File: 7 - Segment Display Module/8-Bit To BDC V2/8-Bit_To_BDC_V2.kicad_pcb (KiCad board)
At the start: 2 copper layers, 93 x 83 mm, 42 parts, among them J1 Conn_01x08_Pin, J2 Conn_01x02_Pin, U1 AT28C64B-15PU, U2 AT28C64B-15PU, U3 4056, U4 4056, U5 4056

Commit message: PCB Layout modification
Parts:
- removed R30: 330, Resistor_SMD:R_0805_2012Metric_Pad1.20x1.40mm_HandSolder
- added D10: US1M, Diode_SMD:D_SOD-323_HandSoldering, F.Cu at (82.4, 60.3)
- added D11: US1M, Diode_SMD:D_SOD-323_HandSoldering, F.Cu at (86.4, 60.3)
- added D4: US1M, Diode_SMD:D_SOD-323_HandSoldering, F.Cu at (58.4, 60.3)
- added D5: US1M, Diode_SMD:D_SOD-323_HandSoldering, F.Cu at (62.4, 60.3)
- added D6: US1M, Diode_SMD:D_SOD-323_HandSoldering, F.Cu at (66.4, 60.3)
- added D7: US1M, Diode_SMD:D_SOD-323_HandSoldering, F.Cu at (70.4, 60.3)
- added D8: US1M, Diode_SMD:D_SOD-323_HandSoldering, F.Cu at (74.4, 60.3)
- added D9: US1M, Diode_SMD:D_SOD-323_HandSoldering, F.Cu at (78.4, 60.3)
- added R22: 330, Resistor_SMD:R_0805_2012Metric_Pad1.20x1.40mm_HandSolder, F.Cu at (111.5, 52.0)
- moved J2 93.4 mm to (50.5, 31.7)
- moved R29 74.1 mm to (121.0, 30.1), turned to 180 degrees
- moved J1 72.2 mm to (50.0, 53.5)
- moved R28 67.3 mm to (121.0, 34.1), turned to 180 degrees
- moved R1 65.3 mm to (58.3, 64.1), turned to 90 degrees
- moved R9 64.7 mm to (70.0, 30.2)
- moved R10 63.7 mm to (70.0, 34.2)
- moved R11 62.8 mm to (70.0, 38.2)
- moved R2 62.4 mm to (62.3, 64.1), turned to 90 degrees
- moved R12 61.9 mm to (70.0, 42.2)
- moved R13 60.9 mm to (70.0, 46.2)
- moved R27 60.5 mm to (121.0, 38.1), turned to 180 degrees
- moved R14 60.0 mm to (70.0, 50.2)
- moved R3 59.6 mm to (66.3, 64.1), turned to 90 degrees
- moved R15 59.1 mm to (70.0, 54.2)
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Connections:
- J1 pad 1: 1 -> Net-(D4-A)
- J1 pad 2: 2 -> Net-(D5-A)
- J1 pad 3: 3 -> Net-(D6-A)
- J1 pad 4: 4 -> Net-(D7-A)
- J1 pad 5: 5 -> Net-(D8-A)
- J1 pad 6: 6 -> Net-(D9-A)
- J1 pad 7: 7 -> Net-(D10-A)
- J1 pad 8: 8 -> Net-(D11-A)
- R11 pad 1: Net-(U3-a) -> Net-(U3-c)
- R11 pad 2: H-A -> H-C
- R23 pad 1: Net-(U4-g) -> Net-(U5-a)
- R23 pad 2: T-G -> O-A
- R24 pad 1: Net-(U5-a) -> Net-(U5-b)
- R24 pad 2: O-A -> O-B
- R25 pad 1: Net-(U5-b) -> Net-(U5-c)
- R25 pad 2: O-B -> O-C
- R26 pad 1: Net-(U5-c) -> Net-(U5-d)
- R26 pad 2: O-C -> O-D
- R27 pad 1: Net-(U5-d) -> Net-(U5-e)
- R27 pad 2: O-D -> O-E
- R28 pad 1: Net-(U5-e) -> Net-(U5-f)
- R28 pad 2: O-E -> O-F
- R29 pad 1: Net-(U5-f) -> Net-(U5-g)
- R29 pad 2: O-F -> O-G
- R9 pad 1: Net-(U3-c) -> Net-(U3-a)
- R9 pad 2: H-C -> H-A
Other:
- board size 93 x 83 mm -> 99 x 67 mm

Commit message: Small changes
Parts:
- added REF**: MountingHole_2.7mm_M2.5_DIN965, MountingHole:MountingHole_2.7mm_M2.5_DIN965, F.Cu at (133.5, 71.0)
- added REF**: MountingHole_2.7mm_M2.5_DIN965, MountingHole:MountingHole_2.7mm_M2.5_DIN965, F.Cu at (134.0, 20.0)
- added REF**: MountingHole_2.7mm_M2.5_DIN965, MountingHole:MountingHole_2.7mm_M2.5_DIN965, F.Cu at (49.0, 71.0)
- added REF**: MountingHole_2.7mm_M2.5_DIN965, MountingHole:MountingHole_2.7mm_M2.5_DIN965, F.Cu at (50.0, 20.5)
- D10, D11, D4, D5, D6, D7, D8, D9, R1, R10, R11, R12, R13, R14, R15, R16, R17, R18, R19, R2, R20, R21, R22, R23, R24, R25, R26, R27, R28, R29, R3, R4, R5, R6, R7, R8, R9: moved to B.Cu
- moved R22 39.6 mm to (84.0, 23.5)
- moved U4 37.7 mm to (95.9, 23.5), turned to 90 degrees
- moved R16 35.1 mm to (108.0, 23.5)
- moved R21 34.5 mm to (88.0, 23.5)
- moved R15 32.3 mm to (68.5, 22.0), turned to 180 degrees
- moved R17 31.1 mm to (104.0, 23.5)
- moved R20 30.7 mm to (92.0, 23.5)
- moved R18 28.9 mm to (100.0, 23.5)
- moved R19 28.7 mm to (96.0, 23.5)
- moved R14 24.3 mm to (68.5, 26.0), turned to 180 degrees
- moved J1 18.3 mm to (53.5, 35.5)
- moved R13 16.3 mm to (68.5, 30.0), turned to 180 degrees
- moved R9 15.8 mm to (68.5, 46.0), turned to 180 degrees
- moved U1 15.4 mm to (112.0, 60.7)
- moved U2 15.3 mm to (71.3, 60.4)
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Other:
- board size 99 x 67 mm -> 92 x 58 mm

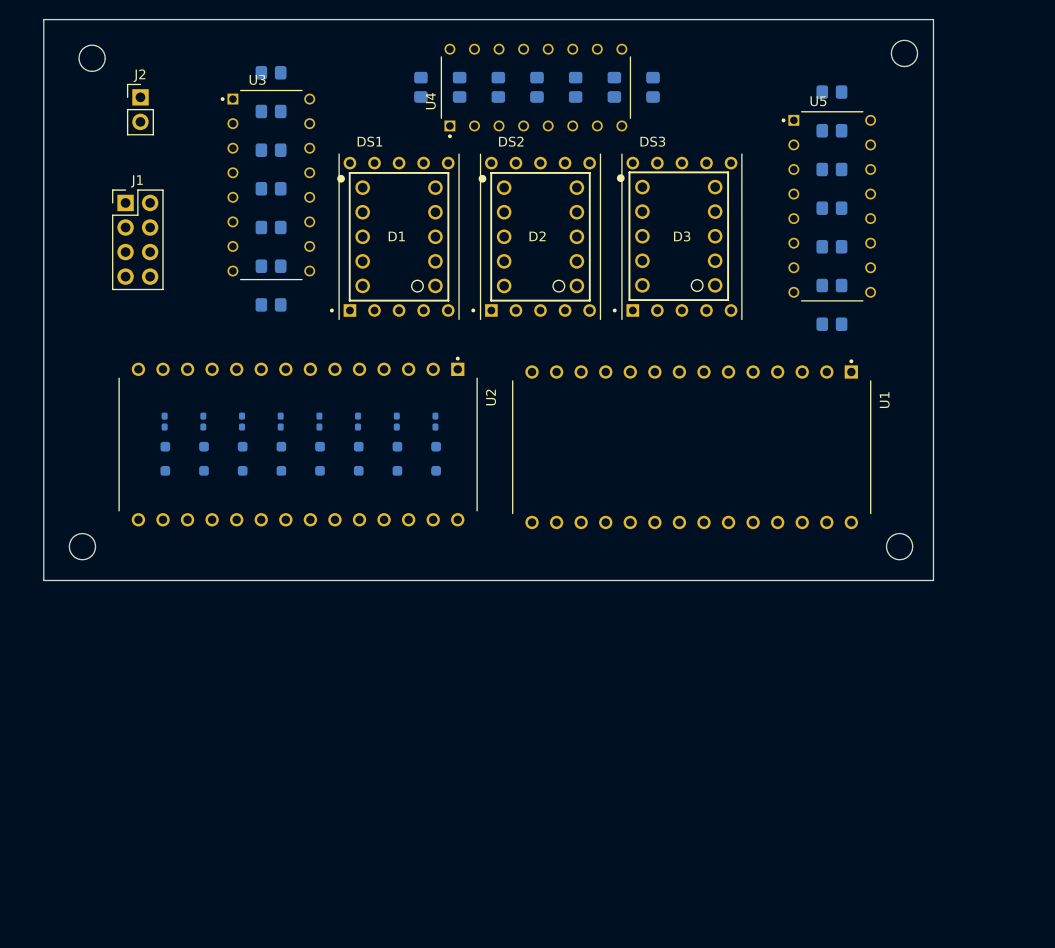
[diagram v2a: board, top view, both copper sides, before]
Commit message: Small changes to fix bugs with new update
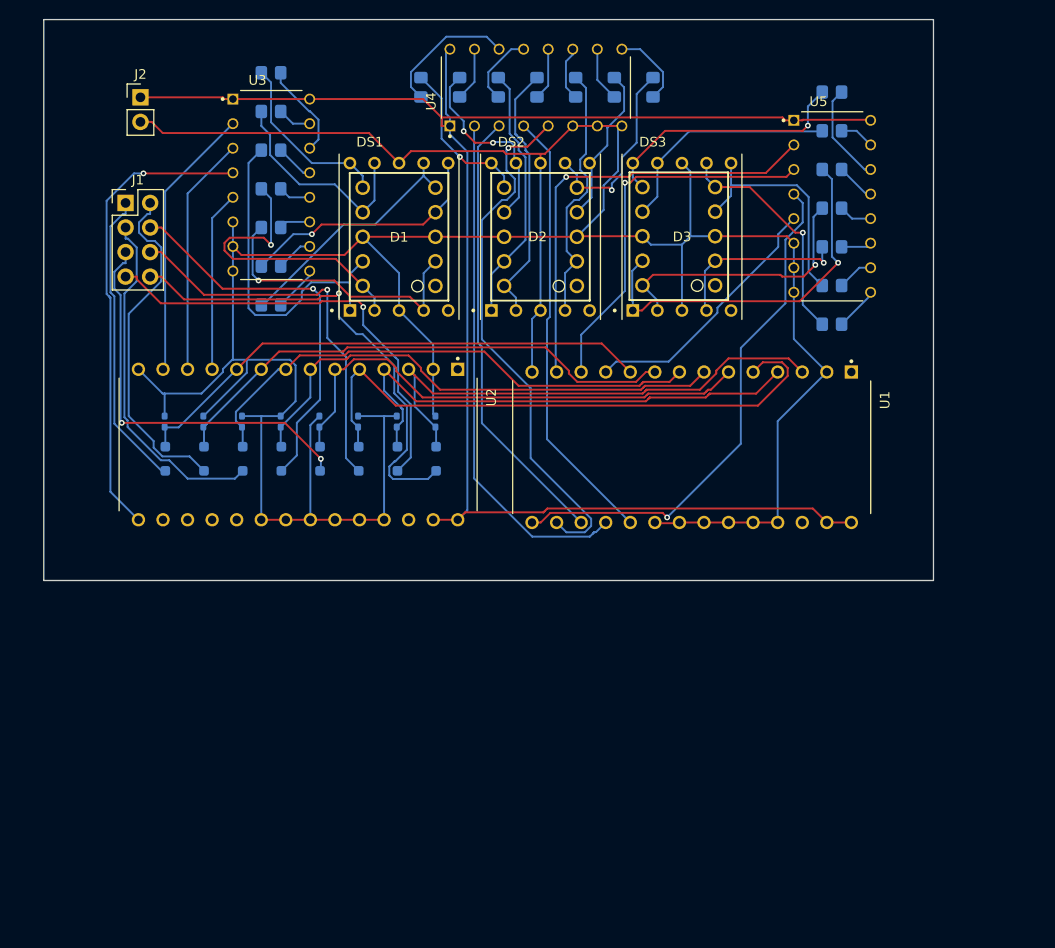
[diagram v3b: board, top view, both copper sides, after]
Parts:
- removed REF** (x4): MountingHole_2.7mm_M2.5_DIN965, MountingHole:MountingHole_2.7mm_M2.5_DIN965
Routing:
- net GND: track 0.00 -> 334.0 mm
- net VCC: track 0.00 -> 173.0 mm
- net 6: track 0.00 -> 60.8 mm
- net T1: track 0.00 -> 55.3 mm, vias 0 -> 1
- net 1: track 0.00 -> 55.0 mm
- net 2: track 0.00 -> 54.7 mm
- net 3: track 0.00 -> 54.6 mm
- net O4: track 0.00 -> 54.2 mm, vias 0 -> 1
- net 4: track 0.00 -> 53.5 mm
- net 8: track 0.00 -> 53.4 mm
- net T3: track 0.00 -> 53.4 mm
- net 5: track 0.00 -> 53.2 mm
- net 7: track 0.00 -> 53.1 mm
- net Net-(D11-A): track 0.00 -> 49.0 mm, vias 0 -> 1
- net H4: track 0.00 -> 48.8 mm, vias 0 -> 1
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
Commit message: Final changes to BCD V2 and switch board
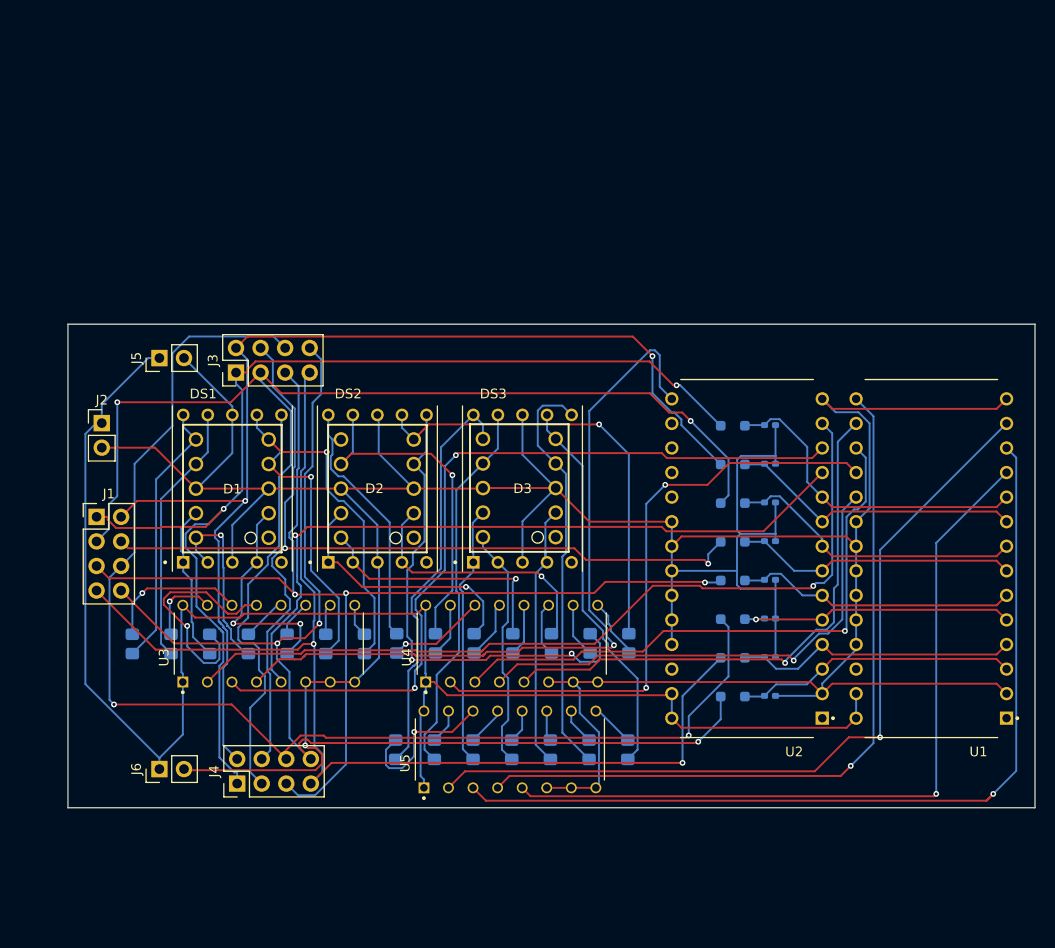
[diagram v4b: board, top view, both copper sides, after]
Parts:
- added J3: Conn_01x08_Pin, Connector_PinHeader_2.54mm:PinHeader_2x04_P2.54mm_Vertical, F.Cu at (64.9, 53.0)
- added J4: Conn_01x08_Pin, Connector_PinHeader_2.54mm:PinHeader_2x04_P2.54mm_Vertical, F.Cu at (65.0, 95.5)
- added J5: Conn_01x02_Pin, Connector_PinHeader_2.54mm:PinHeader_1x02_P2.54mm_Vertical, F.Cu at (57.0, 51.5)
- added J6: Conn_01x02_Pin, Connector_PinHeader_2.54mm:PinHeader_1x02_P2.54mm_Vertical, F.Cu at (57.0, 94.0)
- moved R29 81.6 mm to (81.4, 92.0), turned to -90 degrees
- moved R28 76.1 mm to (85.4, 92.0), turned to -90 degrees
- moved R27 70.5 mm to (89.4, 92.0), turned to -90 degrees
- moved U5 65.3 mm to (93.2, 92.0), turned to 90 degrees
- moved R26 65.1 mm to (93.4, 92.0), turned to -90 degrees
- moved R1 62.6 mm to (120.1, 58.4), turned to 180 degrees
- moved R15 60.8 mm to (54.2, 81.1), turned to -90 degrees
- moved R25 59.6 mm to (97.4, 92.0), turned to -90 degrees
- moved D4 58.8 mm to (116.2, 58.5), turned to 180 degrees
- moved R2 58.8 mm to (120.1, 62.4), turned to 180 degrees
- moved R16 57.6 mm to (105.5, 81.0)
- moved R17 57.6 mm to (101.5, 81.0)
- moved R18 57.6 mm to (97.5, 81.0)
- moved R19 57.6 mm to (93.5, 81.0)
- moved R20 57.6 mm to (89.5, 81.0)
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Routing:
- net Net-(D6-A): track 36.4 -> 137.4 mm, vias 0 -> 2
- net Net-(D9-A): track 40.4 -> 129.5 mm, vias 1 -> 2
- net Net-(D4-A): track 31.1 -> 117.1 mm, vias 0 -> 2
- net Net-(D5-A): track 36.0 -> 118.1 mm, vias 0 -> 2
- net Net-(D10-A): track 46.1 -> 122.0 mm, vias 1 -> 2
- net Net-(D8-A): track 42.0 -> 116.7 mm, vias 2 -> 3
- net Net-(D7-A): track 40.3 -> 111.8 mm, vias 1 -> 2
- net Net-(D11-A): track 49.0 -> 117.3 mm, vias 1 -> 3
- net H2: track 24.8 -> 85.6 mm, vias 0 -> 2
- net H3: track 28.4 -> 85.8 mm, vias 0 -> 1
- net H1: track 18.7 -> 74.8 mm, vias 0 -> 1
- net O2: track 39.5 -> 93.8 mm
- net O1: track 27.1 -> 80.9 mm, vias 0 -> 1
- net GND: track 334.0 -> 375.0 mm, vias 0 -> 1
- net O3: track 45.8 -> 84.7 mm
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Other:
- board size 92 x 58 mm -> 100 x 50 mm
